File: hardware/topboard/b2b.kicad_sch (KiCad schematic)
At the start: 57 parts, among them J1 EDGE_140P, Q1 BSS138, Q2 BSS138, Q3 BSS138, U10 74LVC2T45DC, U11 74LVC2T45DC, U12 74LVC2T45DC, U13 74LVC2T45DC, U14 74AUC1G66, U15 74LVC2T45DC, U9 74LVC2T45DC

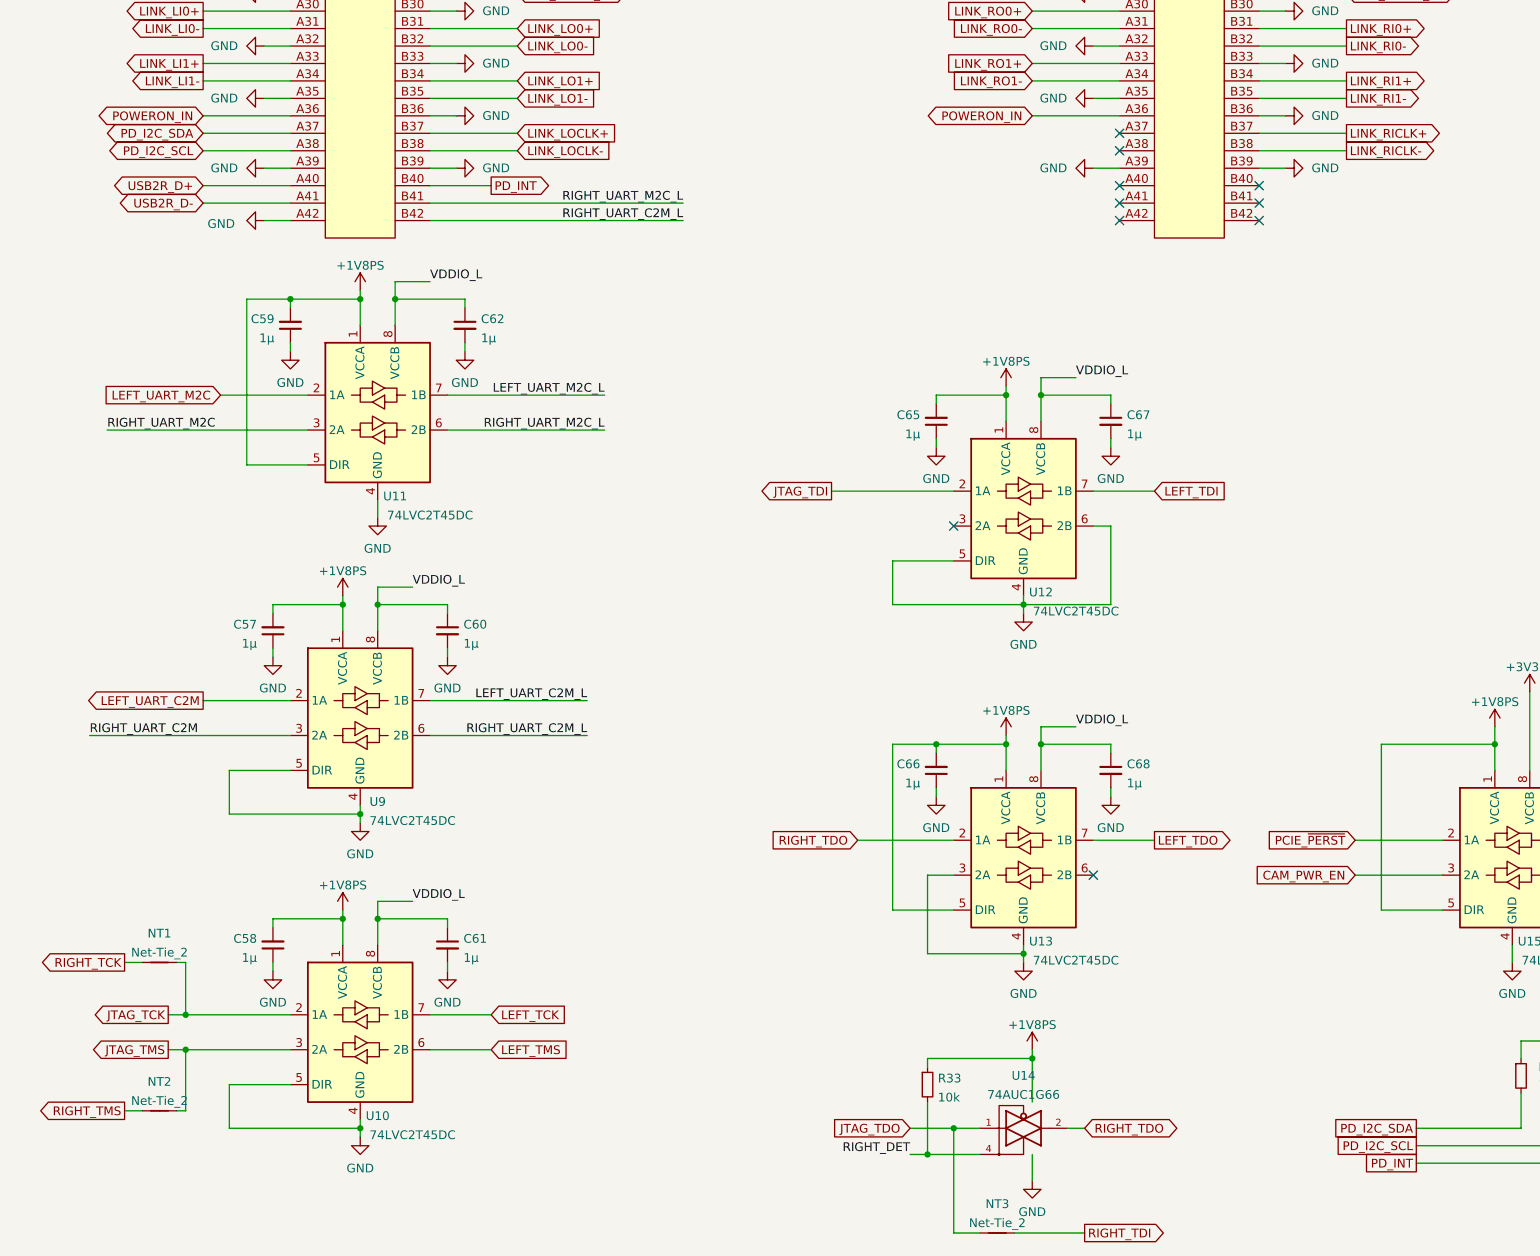
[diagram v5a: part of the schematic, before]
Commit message: Replace type-C power with good ol' barrel jack
Signed-off-by: gatecat <gatecat@ds0.me>
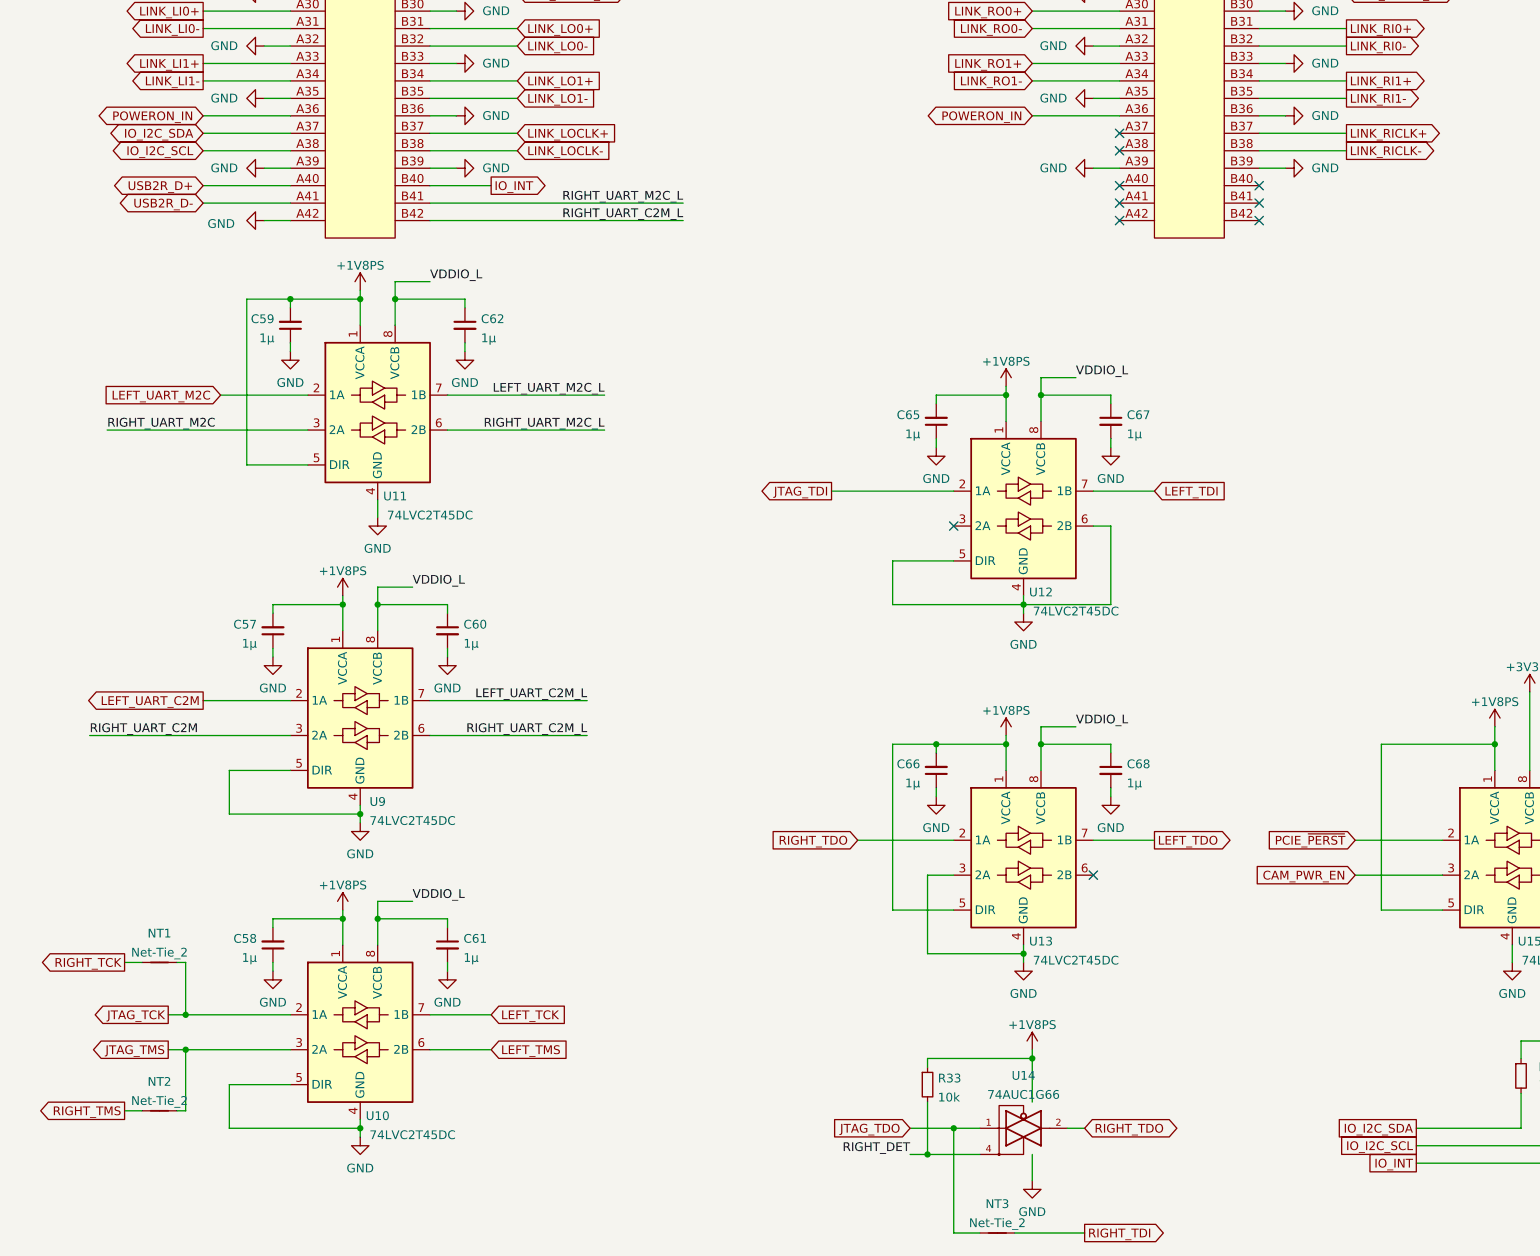
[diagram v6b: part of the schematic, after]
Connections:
- net PD_I2C_SCL renamed IO_I2C_SCL
- net PD_I2C_SDA renamed IO_I2C_SDA
- net PD_INT renamed IO_INT
